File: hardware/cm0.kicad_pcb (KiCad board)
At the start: 4 copper layers, 85 x 60 mm, 177 parts, among them J1 RJ45_Hanrun_HR913550A_Horizon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, J10 AudioJack_PJ-342, J2 GPDI_A, J3 USB_C_Receptacle_USB2.0_14P, J4 USB_C_Receptacle_USB2.0_14P, J5 USB_C_Receptacle_USB2.0_14P, J6 USB_A_Stacked, J7 Micro_SD_Card_Det1, J8 Conn_02x20_Odd_Even, J9 Conn_01x03, Q1 BSN20, Q2 BSN20, Q3 AO3415A, U1 H3, U10 TPD2EUSB30, U11 TPD2EUSB30, U12 TPD2EUSB30, U13 SY6280AAC, U14 SY6280AAC, U15 EMMC5.1_BGA153, U16 TPD2EUSB30, U17 SY8088, U18 SY8088, U19 SY8089A, U2 H5TQ4G63EFR, U20 SY8089A, U21 SY8113, U22 SY8089A, U3 AP6212, U4 UCL0524P, U5 UCL0524P, U6 HUSB237, U7 SY6280AAC, U8 SY6280AAC, U9 TPD2EUSB30, Y1 26MHz

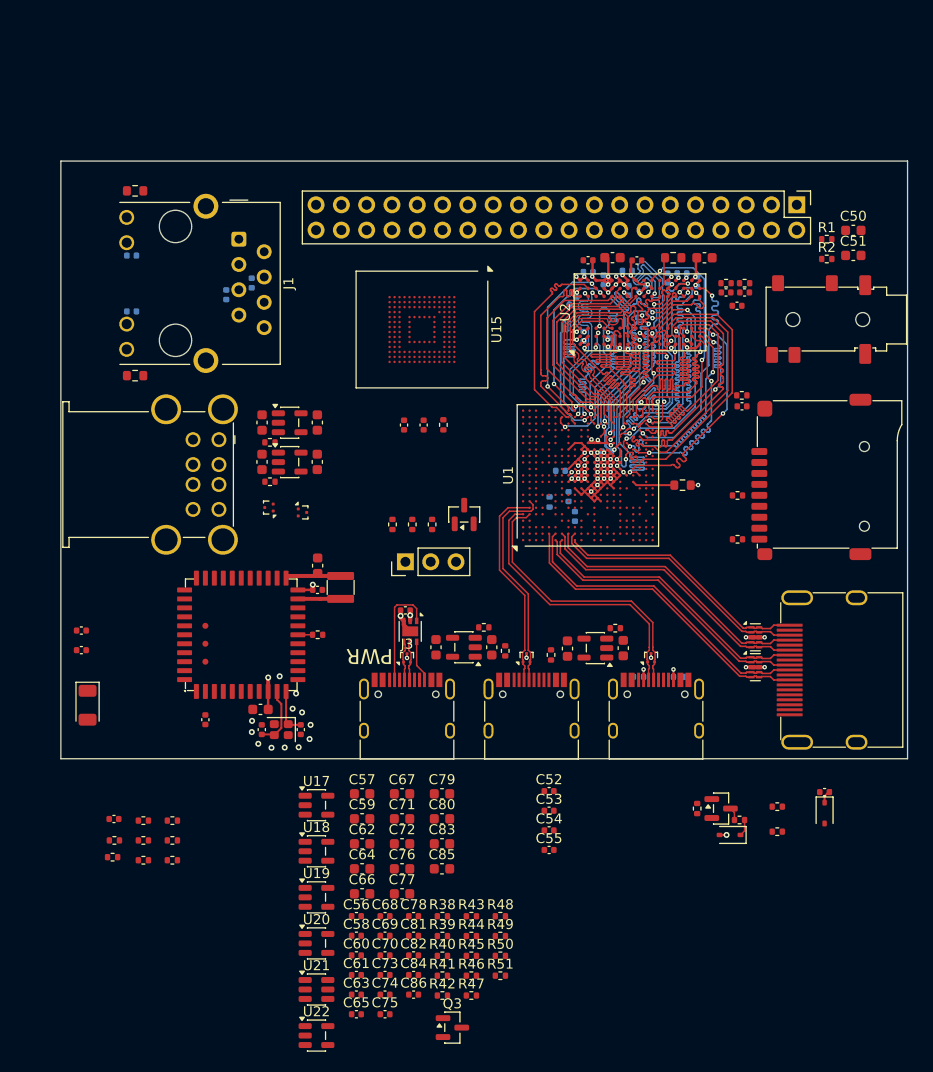
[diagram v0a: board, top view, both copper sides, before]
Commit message: Finished DC DC converters and started decoupling the CPU
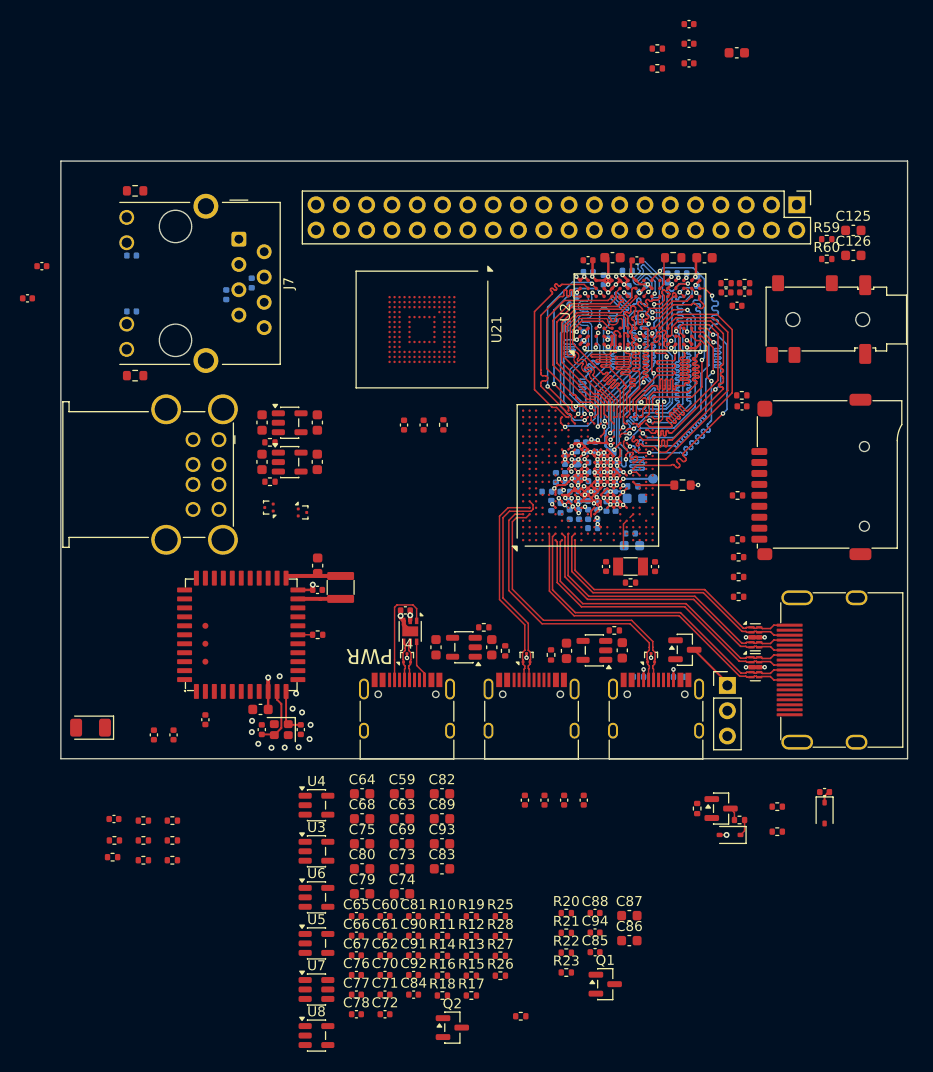
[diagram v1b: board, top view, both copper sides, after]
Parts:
- added C10: 4.7uF, Capacitor_SMD:C_0402_1005Metric, B.Cu at (112.2, 116.5)
- added C11: 4.7uF, Capacitor_SMD:C_0402_1005Metric, B.Cu at (116.4, 120.2)
- added C12: 100nF, Capacitor_SMD:C_0402_1005Metric, B.Cu at (115.9, 121.6)
- added C13: 1uF, Capacitor_SMD:C_0402_1005Metric, B.Cu at (113.1, 114.7)
- added C14: 100nF, Capacitor_SMD:C_0402_1005Metric, B.Cu at (114.3, 113.4)
- added C15: 10uF, Capacitor_SMD:C_0603_1608Metric, B.Cu at (120.1, 118.6)
- added C16: 1uF, Capacitor_SMD:C_0402_1005Metric, B.Cu at (117.3, 119.4)
- added C17: 1uF, Capacitor_SMD:C_0402_1005Metric, B.Cu at (118.2, 119.4)
- added C18: 100nF, Capacitor_SMD:C_0402_1005Metric, B.Cu at (118.1, 117.4)
- added C19: 100nF, Capacitor_SMD:C_0402_1005Metric, B.Cu at (116.8, 117.9)
- added C20: 10uF, Capacitor_SMD:C_0603_1608Metric, B.Cu at (114.3, 115.8)
- added C21: 1uF, Capacitor_SMD:C_0402_1005Metric, B.Cu at (114.9, 117.9)
- added C22: 1uF, Capacitor_SMD:C_0402_1005Metric, B.Cu at (116.0, 115.9)
- added C23: 100nF, Capacitor_SMD:C_0402_1005Metric, B.Cu at (116.0, 116.9)
- added C24: 100nF, Capacitor_SMD:C_0402_1005Metric, B.Cu at (116.0, 115.0)
- added C25: 1uF, Capacitor_SMD:C_0402_1005Metric, B.Cu at (115.9, 118.8)
- added C26: 100nF, Capacitor_SMD:C_0402_1005Metric, B.Cu at (114.1, 118.8)
- added C27: 100nF, Capacitor_SMD:C_0402_1005Metric, B.Cu at (115.4, 120.2)
- added C28: 10uF, Capacitor_SMD:C_0603_1608Metric, B.Cu at (119.8, 123.3)
- added C29: 100nF, Capacitor_SMD:C_0402_1005Metric, B.Cu at (119.7, 122.1)
- added C3: 100nF, Capacitor_SMD:C_0402_1005Metric, B.Cu at (113.6, 120.2)
- added C30: 10uF, Capacitor_SMD:C_0603_1608Metric, F.Cu at (130.4, 73.9)
- added C31: 100nF, Capacitor_SMD:C_0402_1005Metric, F.Cu at (125.6, 74.9)
- added C32: 4.7uF, Capacitor_SMD:C_0402_1005Metric, F.Cu at (125.6, 73.0)
- added C33: 1uF, Capacitor_SMD:C_0402_1005Metric, F.Cu at (125.6, 71.0)
- added C34: 15pF, Capacitor_SMD:C_0402_1005Metric, F.Cu at (122.2, 125.4)
- added C35: 1uF, Capacitor_SMD:C_0402_1005Metric, B.Cu at (115.2, 113.4)
- added C36: 1uF, Capacitor_SMD:C_0402_1005Metric, B.Cu at (117.8, 115.9)
- added C37: 100nF, Capacitor_SMD:C_0402_1005Metric, B.Cu at (117.8, 115.0)
- added C38: 100nF, Capacitor_SMD:C_0402_1005Metric, B.Cu at (116.2, 113.4)
- added C39: 15pF, Capacitor_SMD:C_0402_1005Metric, F.Cu at (117.2, 125.4)
- added C4: 100nF, Capacitor_SMD:C_0402_1005Metric, B.Cu at (111.3, 117.9)
- added C5: 100nF, Capacitor_SMD:C_0402_1005Metric, F.Cu at (59.2, 98.5)
- added C6: 100nF, Capacitor_SMD:C_0402_1005Metric, F.Cu at (60.6, 95.3)
- added C7: 100nF, Capacitor_SMD:C_0402_1005Metric, B.Cu at (113.1, 117.9)
- added C85: 100nF, Capacitor_SMD:C_0402_1005Metric, F.Cu at (116.1, 164.2)
- added C86: 10uF, Capacitor_SMD:C_0603_1608Metric, F.Cu at (119.6, 163.0)
- added C87: 22uF, Capacitor_SMD:C_0603_1608Metric, F.Cu at (119.6, 160.5)
- added C88: 22pF, Capacitor_SMD:C_0402_1005Metric, F.Cu at (116.1, 160.2)
- added C94: NC, Capacitor_SMD:C_0402_1005Metric, F.Cu at (116.1, 162.2)
- added Q1: BSN20, Package_TO_SOT_SMD:SOT-23, F.Cu at (117.2, 167.4)
- added R20: 10k, Resistor_SMD:R_0402_1005Metric, F.Cu at (113.2, 160.2)
- added R21: 11.8K, Resistor_SMD:R_0402_1005Metric, F.Cu at (113.2, 162.2)
- added R22: 30.1k, Resistor_SMD:R_0402_1005Metric, F.Cu at (113.2, 164.2)
- added R23: 10k, Resistor_SMD:R_0402_1005Metric, F.Cu at (113.2, 166.2)
- added R24: 0, Resistor_SMD:R_0402_1005Metric, F.Cu at (108.7, 170.6)
- added R3: 0, Resistor_SMD:R_0402_1005Metric, B.Cu at (119.9, 117.4)
- added R4: 220k, Resistor_SMD:R_0402_1005Metric, F.Cu at (122.4, 73.4)
- added R5: 0, Resistor_SMD:R_0402_1005Metric, F.Cu at (122.4, 75.4)
- added R6: 10M, Resistor_SMD:R_0402_1005Metric, F.Cu at (119.7, 127.0)
- added TP1: TestPoint, TestPoint:TestPoint_Pad_D1.0mm, B.Cu at (122.0, 116.6)
- added Y1: 32kHz, Crystal:Crystal_SMD_3215-2Pin_3.2x1.5mm, F.Cu at (119.7, 125.4)
- moved R56 34.9 mm to (130.6, 124.5), turned to 0 degrees
- moved J8 34.6 mm to (129.4, 137.4), turned to 0 degrees
- moved R57 33.2 mm to (130.6, 126.5), turned to 0 degrees
- moved R58 31.6 mm to (130.6, 128.5), turned to 0 degrees
- moved Q4 26.0 mm to (125.2, 133.8), turned to 0 degrees
- moved C116 14.0 mm to (73.8, 142.3), turned to -90 degrees
- moved C117 11.2 mm to (71.8, 142.3), turned to -90 degrees
- moved C95 6.09 mm to (115.0, 148.9), turned to 90 degrees
- moved C104 3.39 mm to (113.0, 148.9), turned to 90 degrees
- moved C98 2.59 mm to (109.1, 148.9), turned to 90 degrees
- moved AE1 2.27 mm to (65.5, 141.6), turned to 180 degrees
- moved C1 1.41 mm to (112.7, 119.6), turned to 90 degrees
- moved C101 1.16 mm to (111.1, 148.9), turned to 90 degrees
- moved C8 0.82 mm to (113.1, 116.5), turned to -90 degrees
- moved C2 0.45 mm to (114.5, 120.2)
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- renumbered C2 to C1, C43 to C100, C53 to C101, C42 to C102, C44 to C103, C54 to C104, C38 to C105, C40 to C106, C36 to C107, C35 to C108, C45 to C109, C46 to C110, C47 to C111, C28 to C112, C30 to C113, C24 to C114, C31 to C115, C48 to C116, C49 to C117, C34 to C118, C32 to C119, C33 to C120, C25 to C121, C26 to C122, C27 to C123, C29 to C124, C50 to C125, C51 to C126, C3 to C2, C5 to C40, C6 to C41, C9 to C42, C10 to C43, C7 to C44, C8 to C45, C11 to C46, C12 to C47, C13 to C48, C14 to C49, C15 to C50, C16 to C51, C17 to C52, C18 to C53, C20 to C54, C22 to C55, C19 to C56, C21 to C57, C23 to C58, C67 to C59, C68 to C60, C69 to C61, C70 to C62, C71 to C63, C57 to C64, C56 to C65, C58 to C66, C60 to C67, C59 to C68, C72 to C69, C73 to C70, C74 to C71, C75 to C72, C76 to C73, C77 to C74, C62 to C75, C61 to C76, C63 to C77, C65 to C78, C66 to C79, C4 to C8, C64 to C80, C78 to C81, C79 to C82, C85 to C83, C86 to C84, C80 to C89, C1 to C9, C81 to C90, C82 to C91, C84 to C92, C83 to C93, C55 to C95, C37 to C96, C39 to C97, C52 to C98, C41 to C99, J6 to J1, J4 to J2, J5 to J3, J3 to J4, J2 to J5, J7 to J6, J1 to J7, J9 to J8, J8 to J9, L1 to L7, Q3 to Q2, Q1 to Q3, Q2 to Q4, R4 to R1, R38 to R10, R39 to R11, R44 to R12, R45 to R13, R40 to R14, R46 to R15, R41 to R16, R47 to R17, R42 to R18, R43 to R19, R3 to R2, R48 to R25, R51 to R26, R50 to R27, R49 to R28, R23 to R29, R24 to R30, R27 to R31, R29 to R32, R30 to R33, R25 to R34, R26 to R35, R28 to R36, R21 to R37, R22 to R38, R19 to R39, R20 to R40, R34 to R41, R31 to R42, R32 to R43, R33 to R44, R8 to R45, R9 to R46, R10 to R47, R11 to R48, R12 to R49, R13 to R50, R14 to R51, R16 to R52, R15 to R53, R17 to R54, R18 to R55, R37 to R56, R35 to R57, R36 to R58, R1 to R59, R2 to R60, R6 to R7, R7 to R8, R5 to R9, U13 to U10, U14 to U11, U8 to U12, U9 to U13, U11 to U14, U10 to U15, U12 to U16, U6 to U17, U16 to U18, U4 to U19, U5 to U20, U15 to U21, U3 to U22, U18 to U3, U17 to U4, U20 to U5, U19 to U6, U21 to U7, U22 to U8, U7 to U9, Y1 to Y2
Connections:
- net VDD-CPUX renamed +1V1_CPUX
- C1 pad 2: +3V3 -> +3V3_IO
- C2 pad 2: +3V3 -> +3V3_IO
- C77 pad 1: +1V2 -> +1V2_SYSTEM
- C78 pad 2: +1V2 -> +1V2_SYSTEM
- C79 pad 1: +1V2 -> +1V2_SYSTEM
- C8 pad 2: +3V3 -> +3V3_IO
- C80 pad 1: +1V2 -> +1V2_SYSTEM
- R18 pad 2: +1V2 -> +1V2_SYSTEM
- U1 pad F8: unconnected-(U1D-EPHY_VDD-PadF8) -> +1V2_SYSTEM
- U1 pad G10: unconnected-(U1B-VDD-EFUSE-PadG10) -> Net-(U1B-VDD-EFUSE)
- U1 pad G11: +3V3 -> +3V3_IO
- U1 pad G13: VCC-IO -> +3V3_IO
- U1 pad G14: VCC-IO -> +3V3_IO
- U1 pad G15: VCC-IO -> +3V3_IO
- U1 pad G7: unconnected-(U1D-EPHY_VCC-PadG7) -> +3V3_IO
- U1 pad G9: unconnected-(U1D-V33_TV-PadG9) -> +3V3_AVCC
- U1 pad H10: VDD-SYS -> +1V2_SYSTEM
- U1 pad H11: unconnected-(U1B-VDD-EFUSEEBP-PadH11) -> +3V3_IO
- U1 pad H13: VCC-IO -> +3V3_IO
- U1 pad H14: VCC-IO -> +3V3_IO
- U1 pad H7: +3V3 -> +3V3_IO
- U1 pad H8: unconnected-(U1D-GND_TV-PadH8) -> GND
- U1 pad J10: VDD-SYS -> +1V2_SYSTEM
- U1 pad J11: VDD-SYS -> +1V2_SYSTEM
- U1 pad J12: VDD-SYS -> +1V2_SYSTEM
- U1 pad J14: VCC-IO -> +3V3_IO
- U1 pad J15: +3V3 -> +3V3_IO
- U1 pad J6: +3V3 -> +3V3_IO
- U1 pad J7: VDD-CPUS -> VDD_CPUS
- U1 pad J8: VDD-CPUS -> VDD_CPUS
- U1 pad K10: VDD-SYS -> +1V2_SYSTEM
- U1 pad K11: VDD-SYS -> +1V2_SYSTEM
- U1 pad K12: VDD-SYS -> +1V2_SYSTEM
- U1 pad K6: unconnected-(U1G-VCC_RTC-PadK6) -> +3V3_AVCC
- U1 pad L10: VDD-SYS -> +1V2_SYSTEM
- U1 pad L11: VDD-SYS -> +1V2_SYSTEM
- U1 pad L12: VDD-SYS -> +1V2_SYSTEM
- U1 pad L13: VDD-SYS -> +1V2_SYSTEM
- U1 pad L14: VDD-SYS -> +1V2_SYSTEM
- U1 pad M4: unconnected-(U1G-RTC_VIO-PadM4) -> VDD_CPUS
- U1 pad N3: unconnected-(U1G-VCC_PLL-PadN3) -> +3V3_AVCC
- U1 pad T10: unconnected-(U1B-VDD-CPUFB-PadT10) -> /H3/PWR_CPUFB
- U1 pad T4: unconnected-(U1F-PL6-PadT4) -> /H3/PWR_VSET
- U1 pad T9: GND -> Net-(U1G-GND-CPUFB)
- U1 pad U3: unconnected-(U1H-AGND-PadU3) -> /H3/AGND
- U1 pad U4: unconnected-(U1G-X32KOUT-PadU4) -> /H3/X32KO
- U1 pad V3: unconnected-(U1H-AVCC-PadV3) -> +3V3_AVCC
- U1 pad V4: unconnected-(U1H-VRP-PadV4) -> /H3/VRP
- U1 pad V5: unconnected-(U1G-X32KIN-PadV5) -> /H3/X32KI
- U1 pad W5: unconnected-(U1H-VRA2-PadW5) -> /H3/VRA2
- U1 pad Y4: unconnected-(U1H-VRA1-PadY4) -> /H3/VRA1
- U7 pad 3: unconnected-(U21-FB-Pad3) -> Net-(U7-FB)
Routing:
- net GND: track 80.8 -> 98.3 mm, vias 58 -> 75
- net +1V1_CPUX: track 0.00 -> 15.1 mm, vias 0 -> 8
- net +1V2_SYSTEM: track 0.00 -> 15.0 mm, vias 0 -> 8
- net +3V3_IO: track 0.00 -> 11.2 mm, vias 0 -> 8
- net VDD-SYS: track 11.0 -> 0.00 mm, vias 7 -> 0
- net Net-(J8-Pin_1): track 0.00 -> 4.96 mm
- net /H3/PWR_CPUFB: track 0.00 -> 3.42 mm, vias 0 -> 1
- net /H3/X32KO: track 0.00 -> 2.94 mm
- net VDD_CPUS: track 0.00 -> 2.67 mm, vias 0 -> 3
- net +1V5: track 30.4 -> 32.9 mm
- net /GPDI/GPDI_D0-: track 29.6 -> 31.2 mm
- net /GPDI/GPDI_D2-: track 26.9 -> 28.6 mm
- net /GPDI/GPDI_D2+: track 25.7 -> 27.3 mm
- net /GPDI/GPDI_D1-: track 28.5 -> 30.2 mm
- net /GPDI/GPDI_D0+: track 29.1 -> 30.7 mm
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
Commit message: Decoupling on PCB side almost done
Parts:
- removed C5, C6: 100nF, Capacitor_SMD:C_0402_1005Metric
- added C127: 15pF, Capacitor_SMD:C_0402_1005Metric, F.Cu at (121.0, 127.0)
- added C128: 15pF, Capacitor_SMD:C_0402_1005Metric, F.Cu at (117.1, 127.0)
- added C129: 4.7uF, Capacitor_SMD:C_0402_1005Metric, B.Cu at (138.9, 115.2)
- added C130: 100nF, Capacitor_SMD:C_0402_1005Metric, B.Cu at (138.9, 113.3)
- added L1: 2.2uH, Inductor_SMD:L_Sunlord_SWPA3015S, B.Cu at (63.0, 163.8)
- added L2: 2.2uH, Inductor_SMD:L_Sunlord_SWPA3015S, B.Cu at (63.0, 159.3)
- added L3: 2.2uH, Inductor_SMD:L_Sunlord_SWPA3015S, B.Cu at (63.0, 154.7)
- added L4: 2.2uH, Inductor_SMD:L_Sunlord_SWPA4030S, B.Cu at (68.2, 163.3)
- added L5: 2.2uH, Inductor_SMD:L_Sunlord_SWPA4030S, B.Cu at (68.2, 157.8)
- added L6: 2.2uH, Inductor_SMD:L_Sunlord_SWPA3015S, B.Cu at (63.0, 150.2)
- added Q5: MMBT3904, Package_TO_SOT_SMD:SOT-23, B.Cu at (139.9, 118.4)
- added R61: 47k, Resistor_SMD:R_0402_1005Metric, F.Cu at (126.1, 119.9)
- added R62: 100k, Resistor_SMD:R_0402_1005Metric, F.Cu at (126.0, 121.6)
- added R63: 10k, Resistor_SMD:R_0402_1005Metric, B.Cu at (136.0, 119.7)
- added R64: 10k, Resistor_SMD:R_0402_1005Metric, B.Cu at (136.0, 117.7)
- added R65: 10k, Resistor_SMD:R_0402_1005Metric, B.Cu at (136.0, 115.7)
- added R66: 47k, Resistor_SMD:R_0402_1005Metric, B.Cu at (119.5, 123.6)
- added R67: 47k, Resistor_SMD:R_0402_1005Metric, B.Cu at (121.3, 121.2)
- added R68: 47k, Resistor_SMD:R_0402_1005Metric, B.Cu at (118.5, 123.6)
- added R69: 100k, Resistor_SMD:R_0402_1005Metric, B.Cu at (79.6, 163.1)
- added R70: 100k, Resistor_SMD:R_0402_1005Metric, B.Cu at (79.6, 161.1)
- added TP2: TestPoint, TestPoint:TestPoint_Pad_D1.0mm, F.Cu at (110.6, 127.0)
- added TP3: TestPoint, TestPoint:TestPoint_Pad_D1.0mm, F.Cu at (111.8, 128.6)
- added U23: UCL0524P, Package_DFN_QFN:Diodes_UDFN-10_1.0x2.5mm_P0.5mm, F.Cu at (133.2, 136.5)
- added Y3: 24MHz, Crystal:Crystal_SMD_2016-4Pin_2.0x1.6mm, F.Cu at (119.1, 127.0)
- C101, C104, C30, C31, C32, C33, C59, C60, C61, C62, C63, C64, C65, C66, C67, C68, C69, C70, C71, C72, C73, C74, C75, C76, C77, C78, C79, C80, C81, C82, C83, C84, C85, C86, C87, C88, C89, C90, C91, C92, C93, C94, C95, C98, D1, Q1, Q2, Q3, R10, R11, R12, R14, R15, R16, R18, R19, R20, R21, R22, R23, R24, R25, R27, R28, R37, R38, R4, R5, U3, U4, U6, U7: moved to B.Cu
- L7: value 4.7uH -> 2.2uH; footprint cm0:L_SMD_3.0x3.0 -> Inductor_SMD:L_Sunlord_SWPA3015S
- R13, R17, R26: value 2.21k -> 2.2k; moved to B.Cu
- R51: value 100k -> 10k; moved to B.Cu
- U5, U8: value SY8089A -> SY8088; moved to B.Cu
- moved R39 63.9 mm to (87.6, 106.0)
- moved R40 63.9 mm to (87.6, 108.5)
- moved J8 53.1 mm to (89.8, 102.0), turned to 180 degrees
- moved C33 51.3 mm to (123.1, 122.2), turned to 180 degrees
- moved C30 51.2 mm to (120.7, 124.1), turned to -90 degrees
- moved R5 49.2 mm to (124.1, 124.6)
- moved C32 48.4 mm to (123.1, 121.3)
- moved C31 47.4 mm to (121.2, 122.2), turned to 180 degrees
- moved R4 46.4 mm to (123.8, 119.8), turned to -90 degrees
- moved Q4 43.2 mm to (91.2, 107.2), turned to 90 degrees
- moved R46 28.5 mm to (90.2, 137.1)
- moved R47 27.0 mm to (90.2, 134.1)
- moved R48 27.0 mm to (90.2, 132.1)
- moved R50 27.0 mm to (90.2, 136.1)
- moved Q2 24.0 mm to (101.8, 147.7)
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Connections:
- C112 pad 1: +3V3 -> +3V3_WIFI
- C113 pad 1: +3V3 -> +3V3_WIFI
- C114 pad 1: +3V3 -> +3V3_WIFI
- R45 pad 1: +3V3 -> +3V3_WIFI
- R46 pad 1: +3V3 -> +3V3_WIFI
- R47 pad 1: +3V3 -> +3V3_WIFI
- R48 pad 1: +3V3 -> +3V3_WIFI
- R49 pad 1: +3V3 -> +3V3_WIFI
- R50 pad 1: +3V3 -> +3V3_WIFI
- R51 pad 1: +3V3 -> +3V3_WIFI
- R51 pad 2: /H3/WL_HOST_WAKE -> /H3/WIFI_32K
- R52 pad 1: +3V3 -> /H3/WL_REG_ON
- R52 pad 2: /H3/WL_REG_ON -> GND
- U1 pad A1: unconnected-(U1G-JTAG-SEL0-PadA1) -> Net-(U1G-JTAG-SEL0)
- U1 pad AA3: /H3/AUDIO_L -> /Audio/AUDIO_L
- U1 pad AA5: unconnected-(U1G-KEYADC-PadAA5) -> /H3/KEYADC
- U1 pad AA6: unconnected-(U1G-NMI-PadAA6) -> Net-(U1G-NMI)
- U1 pad B2: unconnected-(U1G-JTAG-SEL1-PadB2) -> Net-(U1G-JTAG-SEL1)
- U1 pad K1: unconnected-(U1G-X24MOUT-PadK1) -> /H3/X24MO
- U1 pad K2: unconnected-(U1G-X24MIN-PadK2) -> /H3/X24MI
- U1 pad N2: unconnected-(U1F-PL4-PadN2) -> /H3/RECOVERY
- U1 pad R1: unconnected-(U1F-PL3-PadR1) -> /H3/PWR_KEY
- U1 pad V6: unconnected-(U1G-RESET-PadV6) -> /H3/RESET
- U1 pad W6: unconnected-(U1G-UBOOT-PadW6) -> /H3/UBOOT
- U1 pad Y3: /H3/AUDIO_R -> /Audio/AUDIO_R
- U22 pad 22: +3V3 -> +3V3_WIFI
- U22 pad 9: +3V3 -> +3V3_WIFI
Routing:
- net /USB/USB_VBUS0: track 0.00 -> 15.6 mm
- net /H3/X32KI: track 0.52 -> 10.9 mm
- net /Audio/AUDIO_L: track 0.00 -> 7.51 mm
- net /Audio/AUDIO_R: track 0.00 -> 7.19 mm
- net Net-(D2-K): track 1.53 -> 8.50 mm
- net /H3/X32KO: track 2.94 -> 9.70 mm
- net /H3/X24MI: track 0.00 -> 6.75 mm
- net Net-(J8-Pin_1): track 4.96 -> 0.00 mm
- net +3V3: track 5.65 -> 0.70 mm, vias 3 -> 1
- net /H3/X24MO: track 0.00 -> 4.42 mm
- net /GPDI/GPDI_HPD: track 0.00 -> 4.15 mm
- net /GPDI/GPDI_SCL: track 0.00 -> 3.95 mm
- net /GPDI/GPDI_SDA: track 0.00 -> 3.92 mm
- net /GPDI/GPDI_CECI: track 1.32 -> 5.24 mm
- net Net-(U22-XTAL_OUT): track 4.76 -> 1.40 mm
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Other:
- board size 85 x 60 mm -> 85 x 56 mm
